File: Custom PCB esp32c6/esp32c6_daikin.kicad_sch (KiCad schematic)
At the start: 23 parts, among them J2 Conn_01x05, Q1 BSS138PS, U1 TPS562246, U2 XIAO-ESP32-C6

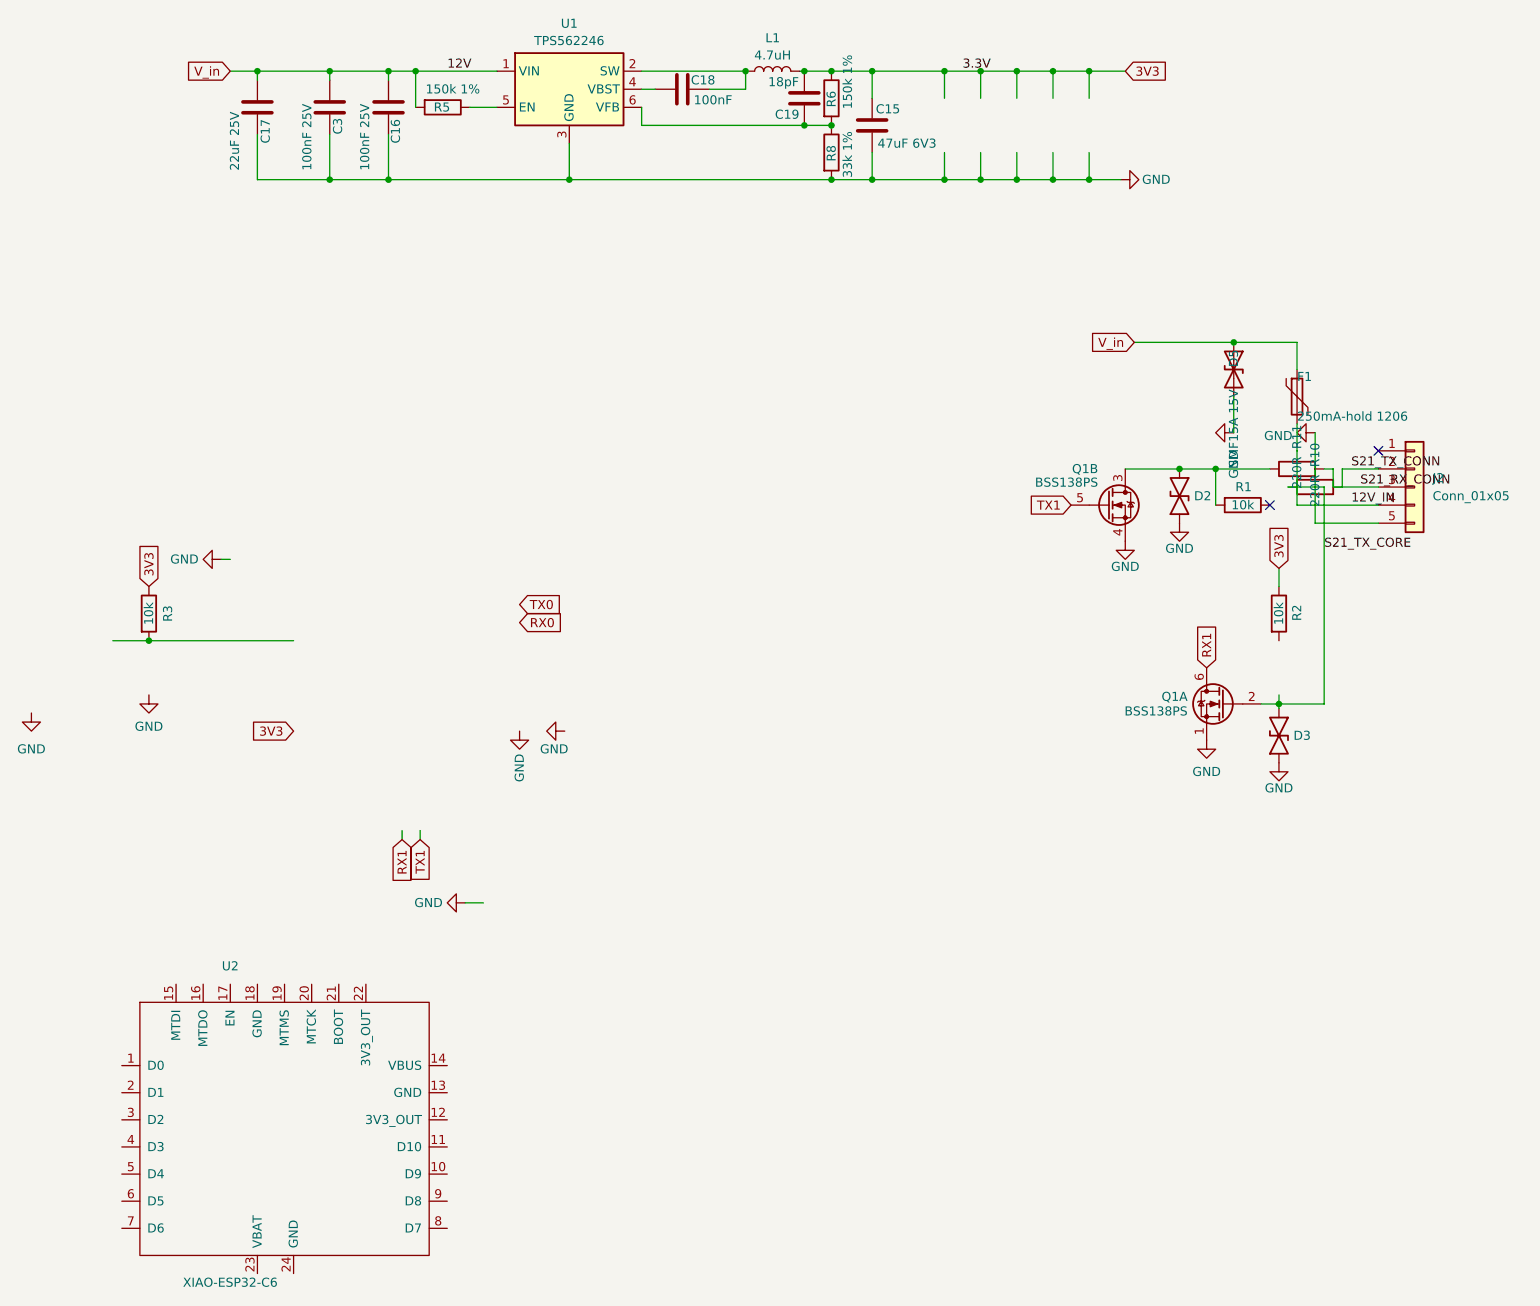
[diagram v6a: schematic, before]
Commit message: feat(xiao-sch): non-inverting AN10441 level shifter + XIAO UART
Replace the old common-source (INVERTING) BSS138PS shifter with the
hardware-validated non-inverting NXP AN10441 gate-shifter, and wire the
XIAO ESP32-C6 UART + power.

Per channel: gate->3V3, source->LV (TX1/RX1, 10k pull-up to 3V3),
drain->HV (10k pull-up to 5V_BUCK) -> 220R (R10/R11) -> J2. Crossed so
XIAO TX (D6) drives aircon Rx (J2 pin3) and aircon Tx (J2 pin2) drives
XIAO RX (D7). Firmware stays invert:false.

- Q1 rewired to AN10441; all vestiges of the inverting wiring removed
  (Q1 source/drain no longer to GND; old /S21_TX_CORE + Q1B-SP nets gone).
- Four 10k pull-ups: R2/R3 kept on 3V3 (LV), R1 repurposed + R12 added
  on 5V_BUCK (HV). 5V_BUCK floats until Task 5 renames the buck output.
- R10->J2 pin3, R11->J2 pin2 (swapped from rev-b to match TX/RX crossing);
  R10/R11 endpoints verified on distinct nets (no net-merge).
- D2/D3 ESD reconnected to the S21 connector lines (spec: ESD on S21),
  keeping HV drain node-sets clean.
- Plan-completion: XIAO 3V3_OUT(12)->3V3, GND(13)->GND wired; VBUS(14)
  left floating for the Task-5 isolation Schottky.

Verified by netlist node-sets (21/21 pass). ERC 149->134 (no new real
violation; +1 footprint_link is R12's lib-path artifact). ERC-0 is Task 5.
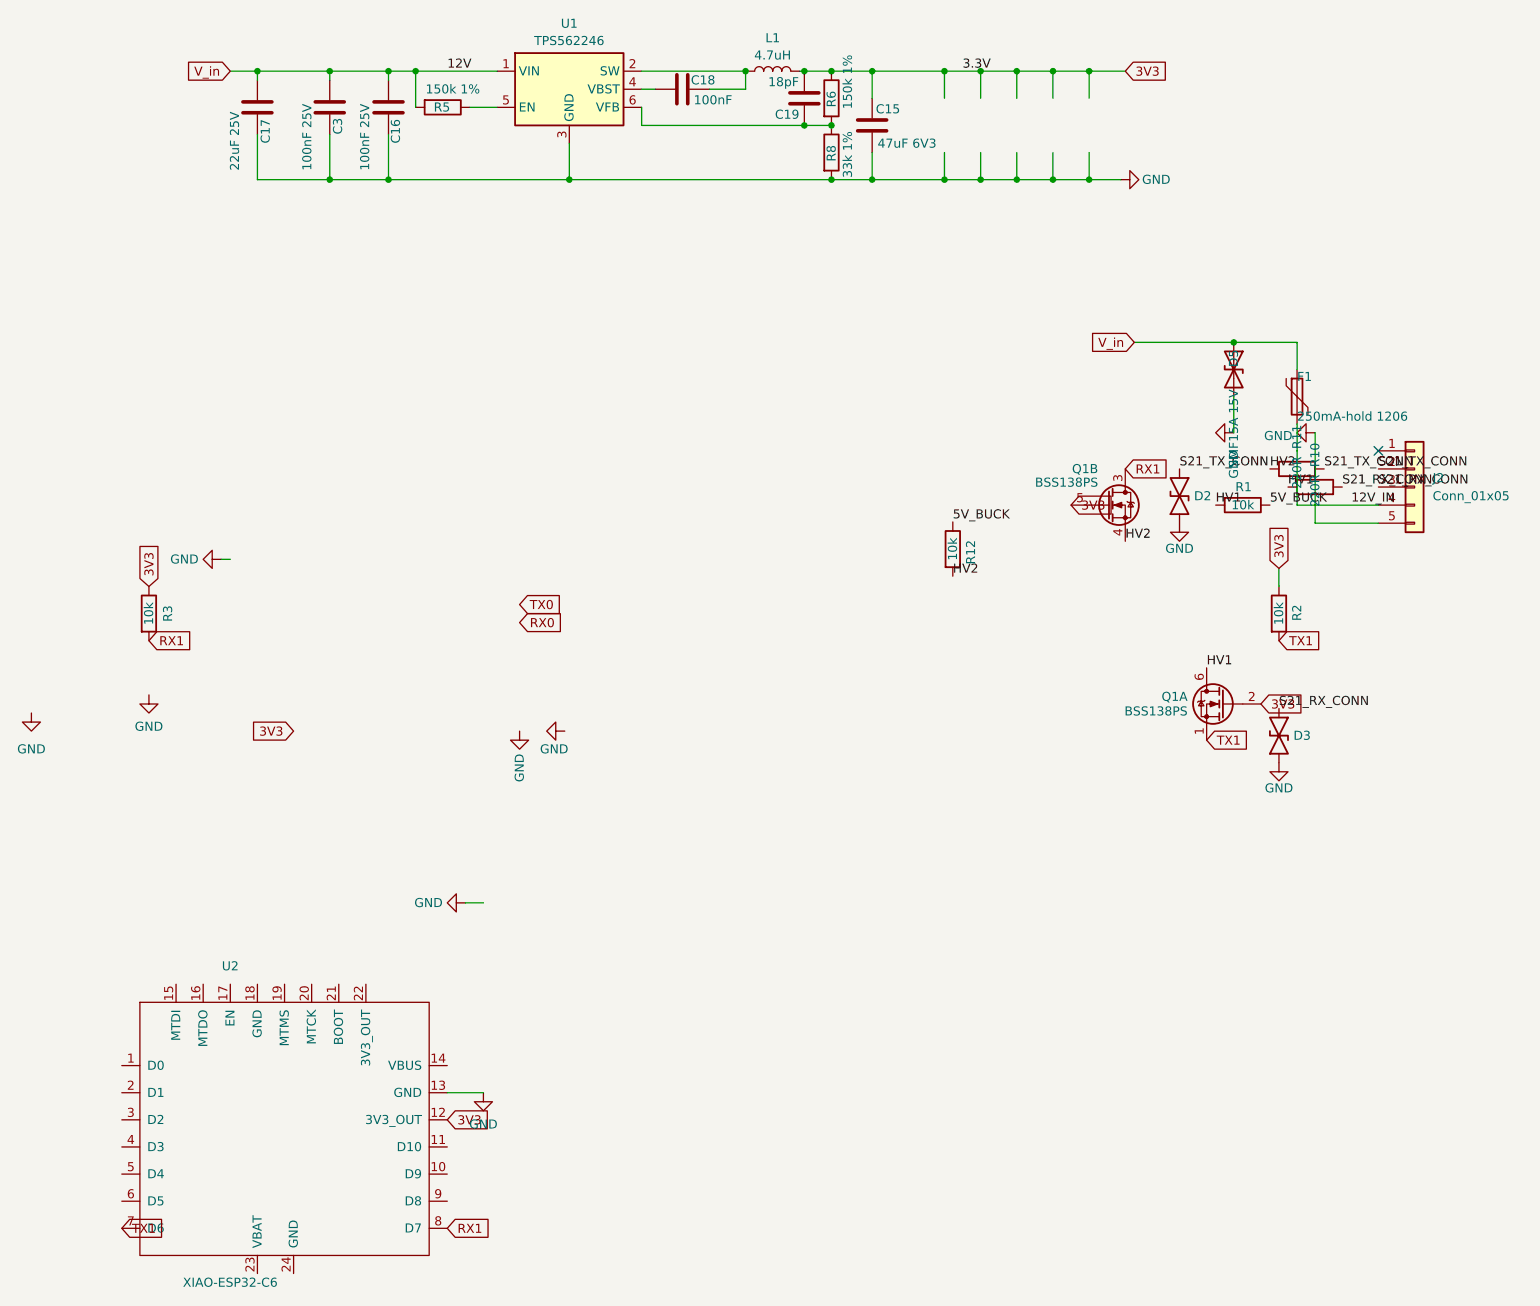
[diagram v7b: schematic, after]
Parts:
- added R12: 10k, easyeda2kicad:R0402, symbol Device:R
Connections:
- net 3V3: now also Q1.2 (GN), Q1.5 (GP), U2.12 (3V3_OUT)
- net GND: now also U2.13 (GND); no longer Q1.1 (SN), Q1.4 (DP)
- net RX1: now also Q1.3 (SP), R3.2, U2.8 (D7); no longer Q1.6 (DN)
- net S21_RX_CONN: now also D3.2, R10.2; no longer R11.2
- net S21_TX_CONN: now also D2.2, R11.2; no longer R10.2
- net TX1: now also Q1.1 (SN), R2.2, U2.7 (D6); no longer Q1.5 (GP)
- net 5V_BUCK: now reaches R1.1
- net 5V_BUCK: now also R12.1
- removed net S21_TX_CORE: D3.2, Q1.2 (GN), R10.1
- new net HV1: Q1.6 (DN), R1.2, R10.1
- new net HV2: Q1.4 (DP), R11.1, R12.2
- no-connect marks 2 -> 1

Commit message: fix(xiao-sch): correct FET-2 source/drain swap in level shifter
Q1 (BSS138PS dual N-MOSFET) channel 2 had RX1/HV2 on the wrong pins.
The RevK symbol names pin 3 "SP" and pin 4 "DP" as if pin3=source,
pin4=drain, but the Nexperia BSS138PS datasheet Table 2 gives the
physical pinout as pin 3 = Drain 2, pin 4 = Source 2 (symbol names are
transposed vs the datasheet). Task 4 wired channel 2 by the symbol's
names, so the low-voltage line (RX1) landed on the physical drain and
the 5V line (HV2) on the physical source, backwards for an AN10441
shifter and opposite to the correct channel 1.

Fix: swap the two labels at Q1 pins 3/4 so RX1 (LV, to XIAO D7) sits on
pin 4 (physical Source 2) and HV2 (HV) on pin 3 (physical Drain 2),
mirroring channel 1. Both body diodes now point LV->HV.

Verified by exported netlist (ground truth):
  RX1 = {U2.8, Q1.4, R3.2}   HV2 = {Q1.3, R11.1, R12.2}
Channel 1 unchanged; R10/R11 endpoints remain on distinct nets; only
RX1 and HV2 node-sets changed, no net merged, no new disconnected net.
ERC unchanged at 134 (no regression). Gate (pin 5) stays on 3V3.

Footprint pad numbering: assigned footprint is the external
easyeda2kicad SOT-363 lib (not on disk); relied on datasheet Table 2
plus the pre-edit common-source corroboration (pin 4 tied to GND in the
original inverter, valid only if pin 4 is the source). KiCad's standard
SOT-363 confirms non-transposed JEDEC pad numbering (pad N at pin N).
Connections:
- net HV2: now also Q1.3 (SP); no longer Q1.4 (DP)
- net RX1: now also Q1.4 (DP); no longer Q1.3 (SP)
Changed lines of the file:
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@@
 	(global_label "RX1"
 		(shape input)
-		(at 189.23 78.74 0)
+		(at 189.23 88.9 0)
 		(effects
 			(font
@@
 		)
 		(property "Intersheetrefs" "${INTERSHEET_REFS}"
-			(at 189.23 78.74 0)
+			(at 189.23 88.9 0)
 			(hide yes)
 			(show_name no)
@@
 	)
 	(label "HV2"
-		(at 189.23 88.9 0)
+		(at 189.23 78.74 0)
 		(effects
 			(font
